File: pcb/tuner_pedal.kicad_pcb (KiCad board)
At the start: 4 copper layers, 50 x 90 mm, 107 parts, among them J1 9V Battery, J2 9V Barrel Female, J3 UART, J4 Fermion 1.8" TFT LCD, J5 SWD, J6 Potentiometer, J7 Guitar Input, J8 Guitar Output, SW1 NRST, SW2 BOOT0, U1 TPS54302, U2 MCP1700T-3302E/TT, U3 PCM1802DB, U4 STM32F411CEU6, U5 TL072, X1 4.096MHz, Y1 25MHz 9pF

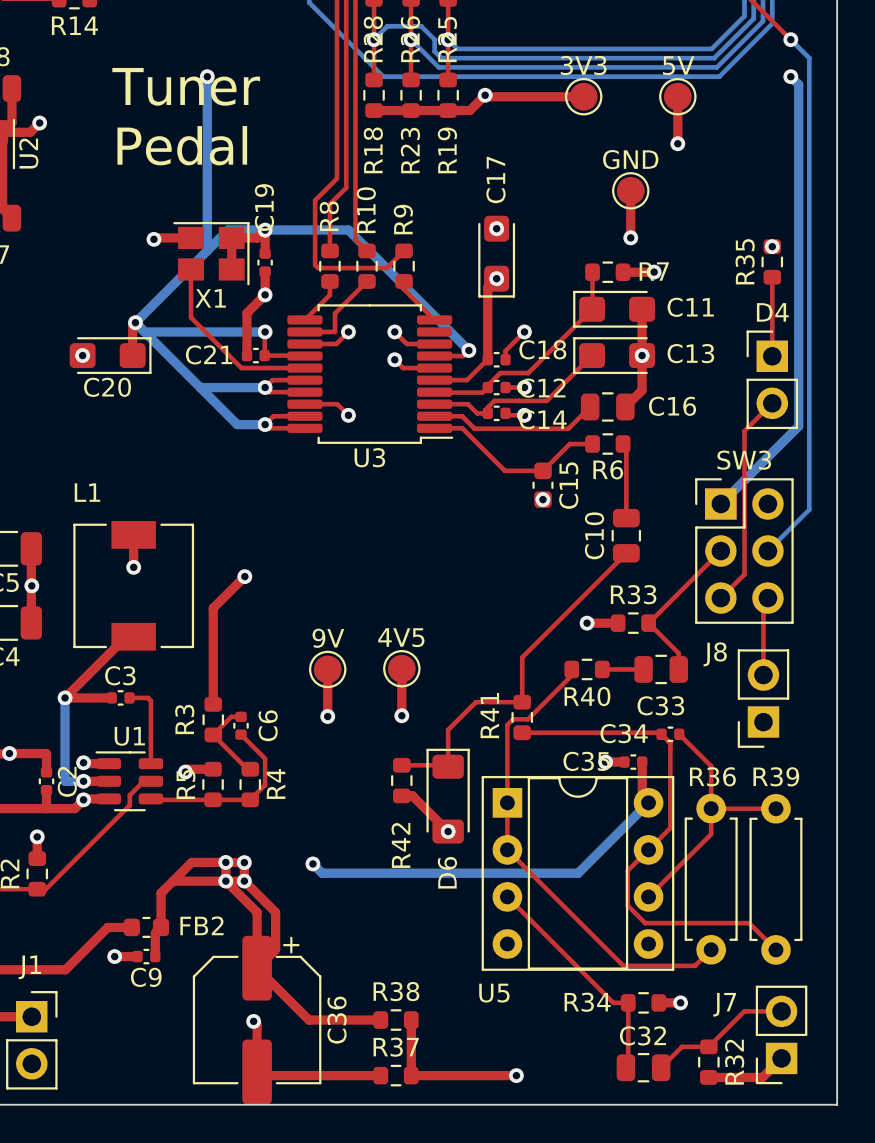
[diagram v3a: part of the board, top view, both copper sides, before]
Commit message: Moved LED to make soldering a bit easier
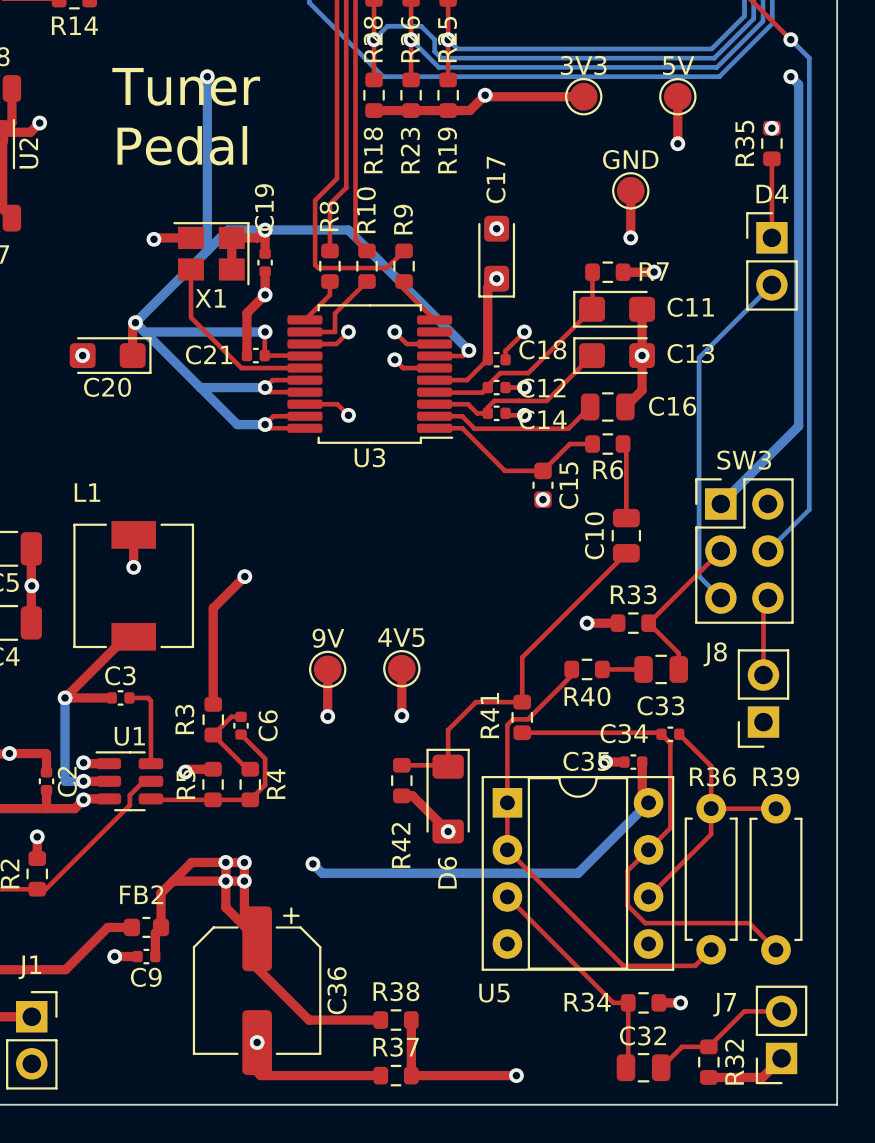
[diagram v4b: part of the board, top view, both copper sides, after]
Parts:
- moved D4 6.39 mm to (157.5, 76.2)
- moved R35 6.39 mm to (157.5, 71.1)
- moved C36 1.59 mm to (129.7, 116.8)
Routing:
- net Net-(D4-A): track 11.7 -> 19.0 mm
- net +9VA: track 68.2 -> 64.2 mm
- net GND: track 123.3 -> 120.5 mm
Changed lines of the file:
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@@
   )
   (footprint "Connector_PinHeader_2.54mm:PinHeader_1x02_P2.54mm_Vertical" (layer "F.Cu")
-    (at 157.5 82.591586)
+    (at 157.48 76.2)
     (descr "Through hole straight pin header, 1x02, 2.54mm pitch, single row")
     (tags "Through hole pin header THT 1x02 2.54mm single row")
@@
   )
   (footprint "Resistor_SMD:R_0603_1608Metric" (layer "F.Cu")
-    (at 157.5 77.5 90)
+    (at 157.48 71.108414 90)
     (descr "Resistor SMD 0603 (1608 Metric), square (rectangular) end terminal, IPC_7351 nominal, (Body size source: IPC-SM-782 page 72, https://www.pcb-3d.com/wordpress/wp-content/uploads/ipc-sm-782a_amendment_1_and_2.pdf), generated with kicad-footprint-generator")
     (tags "resistor")
@@
   )
   (footprint "Capacitor_SMD:CP_Elec_6.3x5.4" (layer "F.Cu")
-    (at 129.6875 118.42625 -90)
+    (at 129.6875 116.84 -90)
     (descr "SMD capacitor, aluminum electrolytic, Panasonic C55, 6.3x5.4mm")
     (tags "capacitor electrolytic")
@@
     (property "ki_keywords" "L ferrite bead inductor filter")
     (attr smd)
-    (fp_text reference "FB2" (at -3 0.04) (layer "F.SilkS")
+    (fp_text reference "FB2" (at 0.255228 1.721623) (layer "F.SilkS")
         (effects (font (size 1 1) (thickness 0.15)))
     )
@@
     (effects (font (size 2 2) (thickness 0.24)) (justify left bottom))
   )
-  (segment (start 129.6875 121.22625) (end 129.6875 118.6875) (width 0.5) (layer "F.Cu") (net 1))
   (segment (start 114.31875 104.0625) (end 116.29375 104.0625) (width 0.5) (layer "F.Cu") (net 1))
   (segment (start 134.55 46.55) (end 134.55 45.7625) (width 0.25) (layer "F.Cu") (net 1))
@@
   (segment (start 145.675 55) (end 144.5 55) (width 0.5) (layer "F.Cu") (net 1))
   (segment (start 154.5 59) (end 154.5 57.325) (width 0.5) (layer "F.Cu") (net 1))
-  (segment (start 129.6875 118.6875) (end 129.5 118.5) (width 0.5) (layer "F.Cu") (net 1))
   (segment (start 138 50.5) (end 139.05 51.55) (width 0.25) (layer "F.Cu") (net 1))
   (segment (start 120.36875 104.5875) (end 120.31875 104.5375) (width 0.5) (layer "F.Cu") (net 1))
@@
   (via (at 150.47 82.555) (size 0.8) (drill 0.4) (layers "F.Cu" "B.Cu") (free) (net 1))
   (via (at 138 49) (size 0.8) (drill 0.4) (layers "F.Cu" "B.Cu") (net 1))
-  (via (at 157.5 76.675) (size 0.8) (drill 0.4) (layers "F.Cu" "B.Cu") (free) (net 1))
+  (via (at 157.48 70.283414) (size 0.8) (drill 0.4) (layers "F.Cu" "B.Cu") (free) (net 1))
   (via (at 149.86 76.2) (size 0.8) (drill 0.4) (layers "F.Cu" "B.Cu") (free) (net 1))
   (via (at 145.12 90.33) (size 0.8) (drill 0.4) (layers "F.Cu" "B.Cu") (free) (net 1))
   (via (at 134.62 81.28) (size 0.8) (drill 0.4) (layers "F.Cu" "B.Cu") (free) (net 1))
-  (via (at 129.5 118.5) (size 0.8) (drill 0.4) (layers "F.Cu" "B.Cu") (free) (net 1))
+  (via (at 129.6875 119.64) (size 0.8) (drill 0.4) (layers "F.Cu" "B.Cu") (free) (net 1))
   (via (at 125.81875 105.0375) (size 0.8) (drill 0.4) (layers "F.Cu" "B.Cu") (free) (net 1))
   (via (at 130.12 79.28) (size 0.8) (drill 0.4) (layers "F.Cu" "B.Cu") (free) (net 1))
@@
   (segment (start 126.156646 109.917104) (end 125.1875 110.88625) (width 0.5) (layer "F.Cu") (net 2))
   (segment (start 136.3625 118.42625) (end 132.4875 118.42625) (width 0.5) (layer "F.Cu") (net 2))
-  (segment (start 129 110.92625) (end 130.6875 112.61375) (width 0.5) (layer "F.Cu") (net 2))
-  (segment (start 130.6875 114.62625) (end 129.6875 115.62625) (width 0.5) (layer "F.Cu") (net 2))
   (segment (start 114.81875 109.7025) (end 114.80875 109.7125) (width 0.5) (layer "F.Cu") (net 2))
+  (segment (start 128 110.92625) (end 128 112.3525) (width 0.5) (layer "F.Cu") (net 2))
   (segment (start 124.1925 115) (end 124.1925 113.73375) (width 0.5) (layer "F.Cu") (net 2))
   (segment (start 132.4875 118.42625) (end 129.6875 115.62625) (width 0.5) (layer "F.Cu") (net 2))
@@
   (segment (start 125.2275 110.92625) (end 125.1875 110.88625) (width 0.5) (layer "F.Cu") (net 2))
   (segment (start 150.48 106.36) (end 150.82 106.7) (width 0.5) (layer "F.Cu") (net 2))
+  (segment (start 129 110.92625) (end 129 113.3525) (width 0.5) (layer "F.Cu") (net 2))
   (segment (start 124.5 111.57375) (end 124.6675 111.40625) (width 0.5) (layer "F.Cu") (net 2))
-  (segment (start 128 110.92625) (end 129.6875 112.61375) (width 0.5) (layer "F.Cu") (net 2))
-  (segment (start 130.6875 112.61375) (end 130.6875 114.62625) (width 0.5) (layer "F.Cu") (net 2))
   (segment (start 133.5 102.04) (end 133.5 99.5) (width 0.5) (layer "F.Cu") (net 2))
   (segment (start 128 110.92625) (end 125.2275 110.92625) (width 0.5) (layer "F.Cu") (net 2))
-  (segment (start 129.6875 112.61375) (end 129.6875 115.62625) (width 0.5) (layer "F.Cu") (net 2))
   (segment (start 114.81875 108.5375) (end 114.81875 109.7025) (width 0.5) (layer "F.Cu") (net 2))
+  (segment (start 128 112.3525) (end 129.6875 114.04) (width 0.5) (layer "F.Cu") (net 2))
   (segment (start 124.5 113.42625) (end 124.5 111.57375) (width 0.5) (layer "F.Cu") (net 2))
   (segment (start 119.84375 107.0125) (end 120.31875 106.5375) (width 0.5) (layer "F.Cu") (net 2))
+  (segment (start 129 113.3525) (end 129.6875 114.04) (width 0.5) (layer "F.Cu") (net 2))
   (segment (start 124.6675 111.40625) (end 125.1875 110.88625) (width 0.5) (layer "F.Cu") (net 2))
   (segment (start 128 109.917104) (end 126.156646 109.917104) (width 0.5) (layer "F.Cu") (net 2))
@@
   (segment (start 137.946701 35.3) (end 136.973299 35.3) (width 0.25) (layer "F.Cu") (net 28))
   (segment (start 147.875 44.875) (end 147.496751 44.875) (width 0.25) (layer "F.Cu") (net 28))
-  (segment (start 157.5 85.131586) (end 156 86.631586) (width 0.25) (layer "F.Cu") (net 29))
-  (segment (start 156 86.631586) (end 156 94.371586) (width 0.25) (layer "F.Cu") (net 29))
-  (segment (start 156 94.371586) (end 154.725 95.646586) (width 0.25) (layer "F.Cu") (net 29))
+  (segment (start 157.48 78.74) (end 153.55 82.67) (width 0.25) (layer "B.Cu") (net 29))
+  (segment (start 153.55 82.67) (end 153.55 94.471586) (width 0.25) (layer "B.Cu") (net 29))
+  (segment (start 153.55 94.471586) (end 154.725 95.646586) (width 0.25) (layer "B.Cu") (net 29))
   (segment (start 117.525 118.25) (end 113.525 118.25) (width 0.5) (layer "F.Cu") (net 30))
   (segment (start 143.325 39.5) (end 143.325 37.175) (width 0.25) (layer "F.Cu") (net 31))
@@
   (segment (start 157.7 114.641586) (end 156.253414 113.195) (width 0.25) (layer "F.Cu") (net 61))
   (segment (start 144 102.916586) (end 151.436586 102.916586) (width 0.25) (layer "F.Cu") (net 61))
-  (segment (start 157.5 82.591586) (end 157.5 78.325) (width 0.25) (layer "F.Cu") (net 62))
+  (segment (start 157.48 76.2) (end 157.48 71.933414) (width 0.25) (layer "F.Cu") (net 62))
   (segment (start 149.46 115.5) (end 143.2 109.24) (width 0.25) (layer "F.Cu") (net 63))
   (segment (start 143.2 102.499124) (end 143.2 106.7) (width 0.25) (layer "F.Cu") (net 63))

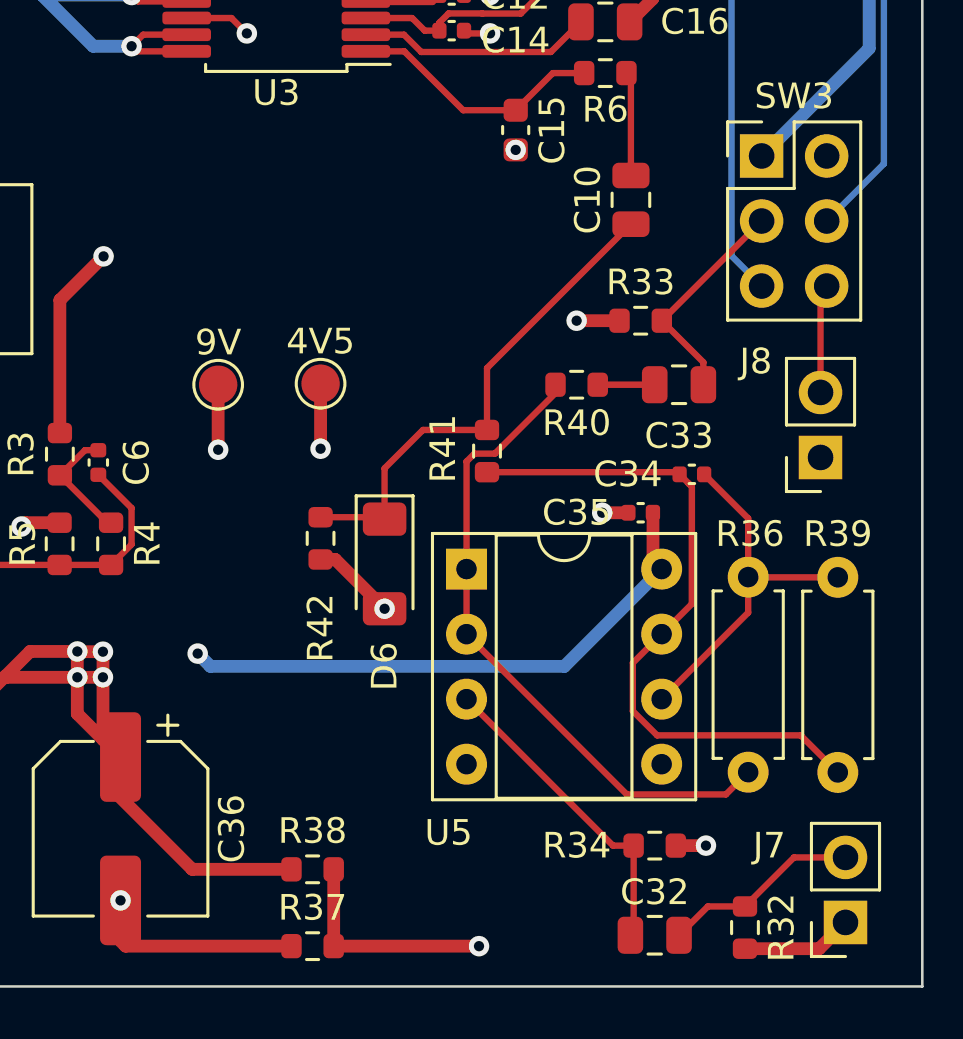
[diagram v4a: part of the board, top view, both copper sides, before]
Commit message: Lowered resistor values and added protection diode
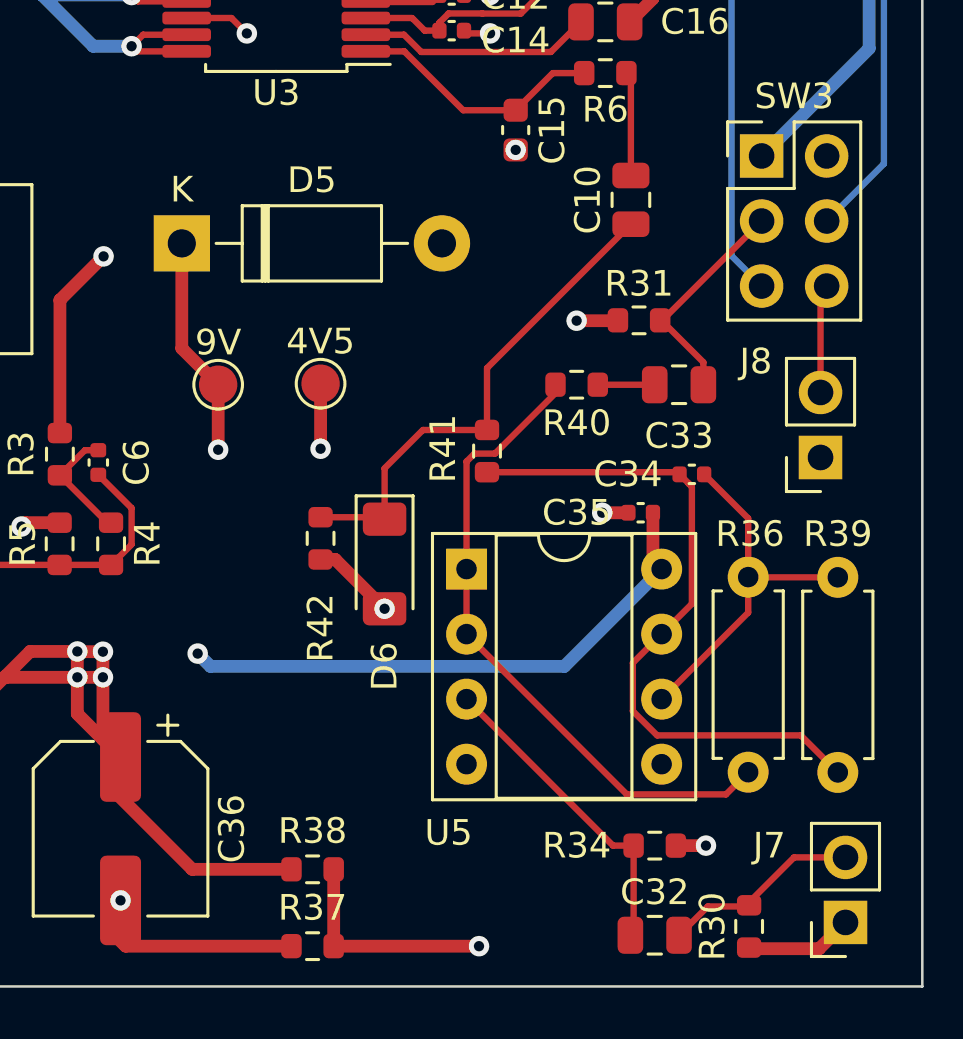
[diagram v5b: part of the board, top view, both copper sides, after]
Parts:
- removed R32, R33: 1Meg, Resistor_SMD:R_0603_1608Metric
- added D5: 1N4004, Diode_THT:D_DO-41_SOD81_P10.16mm_Horizontal, F.Cu at (132.1, 94.0)
- added R30: 100k, Resistor_SMD:R_0603_1608Metric, F.Cu at (154.2, 120.7)
- added R31: 100k, Resistor_SMD:R_0603_1608Metric, F.Cu at (149.9, 97.0)
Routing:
- net +9VA: track 64.2 -> 70.3 mm
